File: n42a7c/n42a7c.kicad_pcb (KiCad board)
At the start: 2 copper layers, 265.5 x 105.1 mm, 111 parts, among them J1 Conn_01x02, J2 Conn_01x03, SW1 CPG151101S11-16, SW10 CPG151101S11-16, SW11 CPG151101S11-16, SW12 CPG151101S11-16, SW13 CPG151101S11-16, SW14 CPG151101S11-16, SW15 CPG151101S11-16, SW16 CPG151101S11-16, SW17 CPG151101S11-16, SW18 CPG151101S11-16, SW19 CPG151101S11-16, SW2 CPG151101S11-16, SW20 CPG151101S11-16, SW21 CPG151101S11-16, SW22 CPG151101S11-16, SW23 CPG151101S11-16, SW24 CPG151101S11-16, SW25 CPG151101S11-16, SW26 CPG151101S11-16, SW27 CPG151101S11-16, SW28 CPG151101S11-16, SW29 CPG151101S11-16, SW3 CPG151101S11-16, SW30 CPG151101S11-16, SW31 CPG151101S11-16, SW32 CPG151101S11-16, SW33 CPG151101S11-16, SW34 CPG151101S11-16, SW35 CPG151101S11-16, SW36 CPG151101S11-16, SW37 CPG151101S11-16, SW38 CPG151101S11-16, SW39 CPG151101S11-16, SW4 CPG151101S11-16, SW40 CPG151101S11-16, SW41 CPG151101S11-16, SW42 CPG151101S11-16, SW5 CPG151101S11-16, SW6 CPG151101S11-16, SW7 CPG151101S11-16, SW8 CPG151101S11-16, SW9 CPG151101S11-16, U1 XIAO-nRF52840-SMD

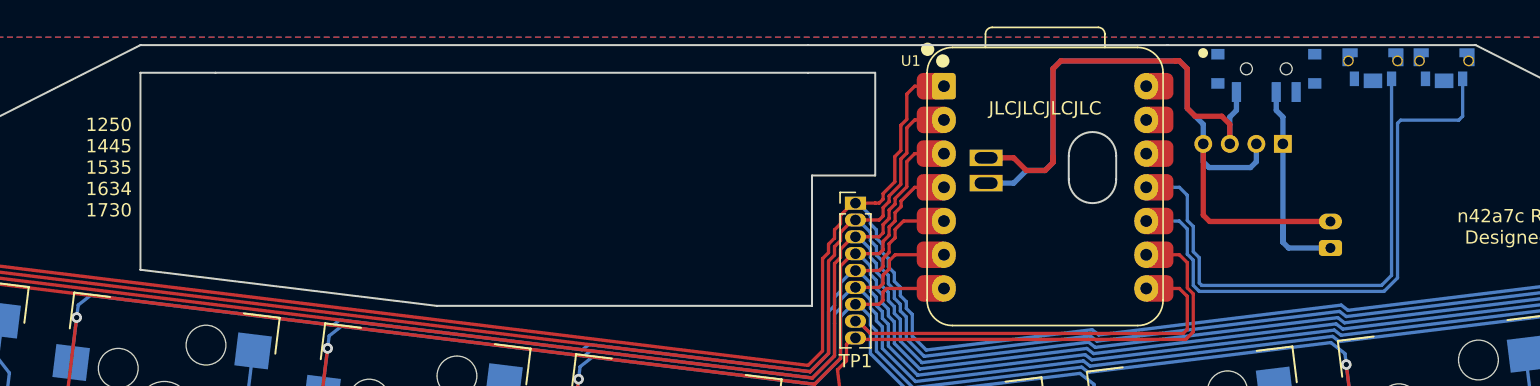
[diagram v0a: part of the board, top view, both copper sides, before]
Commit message: revise power line
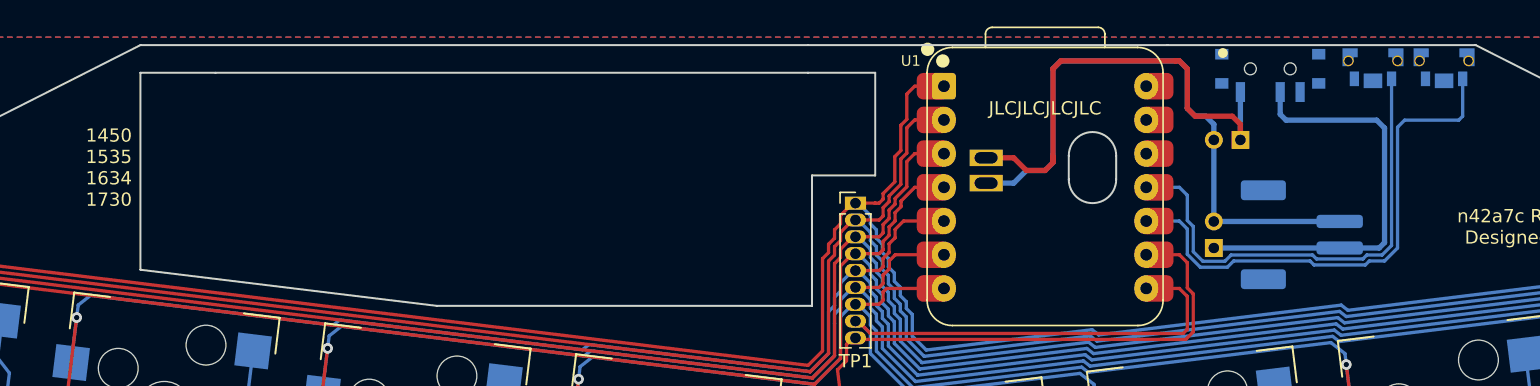
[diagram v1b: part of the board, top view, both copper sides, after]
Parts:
- added J3: S2B-PH-SM4-TB, Connector_PinHeader_2.00mm:PinHeader_1x02_P2.00mm_Vertical, B.Cu at (179.0, 29.8)
- J1: value Conn_01x02 -> S2B-PH-SM4-TB; footprint Connector_JST:JST_PH_S2B-PH-K_1x02_P2.00mm_Horizontal -> Connector_JST:JST_PH_S2B-PH-SM4-TB_1x02-1MP_P2.00mm_Horizontal
- J2: value Conn_01x03 -> S2B-PH-SM4-TB; footprint Connector_PinHeader_2.00mm:PinHeader_1x04_P2.00mm_Vertical -> Connector_PinHeader_2.00mm:PinHeader_1x02_P2.00mm_Vertical
- moved J2 9.41 mm to (177.0, 37.9), turned to 0 degrees
- moved J1 2.37 mm to (183.7, 36.9)
- moved SW_HPWR1 0.30 mm to (181.3, 24.4)
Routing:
- net Net-(J1-Pin_1): track 17.3 -> 32.5 mm
- net BAT-: track 52.7 -> 46.0 mm
- net Fn: track 42.5 -> 38.7 mm
- net PWR: track 40.0 -> 36.3 mm
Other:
- board text added: "1450 1535 1634 1730"
- board text added: "7.0mm spacer"
- board text added: "B+"
- board text added: "B-"
- board text added: "M3x5 ramimate"
- board text added: "PH conn"
- board text added: "foot"
- board text removed: "1250 1445 1535 1634 1730"
- board text removed: "C"

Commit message: revise sw
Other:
- board text removed: "-"
- board text removed: "B-"

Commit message: revise switch
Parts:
- moved SW_DR1 0.60 mm to (188.4, 23.8)
- moved J1 0.42 mm to (183.4, 36.6)
- moved J2 0.42 mm to (176.7, 37.6)
- moved SW_DR2 0.30 mm to (194.1, 23.8)
- moved J3 0.30 mm to (178.7, 29.8)
- moved SW_HPWR1 0.30 mm to (181.0, 24.4)
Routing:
- net Net-(J1-Pin_1): track 32.5 -> 30.8 mm
- net PWR: track 36.3 -> 35.3 mm
- net Fn: track 38.7 -> 37.8 mm
- net BAT-: track 46.0 -> 45.4 mm
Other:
- board text added: "PHconn SMD"
- board text removed: "PH conn"
